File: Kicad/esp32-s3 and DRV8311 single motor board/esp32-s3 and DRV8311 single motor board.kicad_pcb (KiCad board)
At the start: 4 copper layers, 38.8 x 40.3 mm, 90 parts, among them J1 JST SH SM04B, J2 7 pin FPC 0.3mm, J3 Molex_PicoBlade_53048-0310 Ho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, Q3 PMOS,Si7157DP, Q4 PMOS, SW1 SW_Push, SW2 SW_Push, U1 AP2112K-3.3, U2 DRV8311HRRWR, U4 BQ25060, U5 ESP32-S3, U6 74HC595, Y1 40mhz, 10ppm

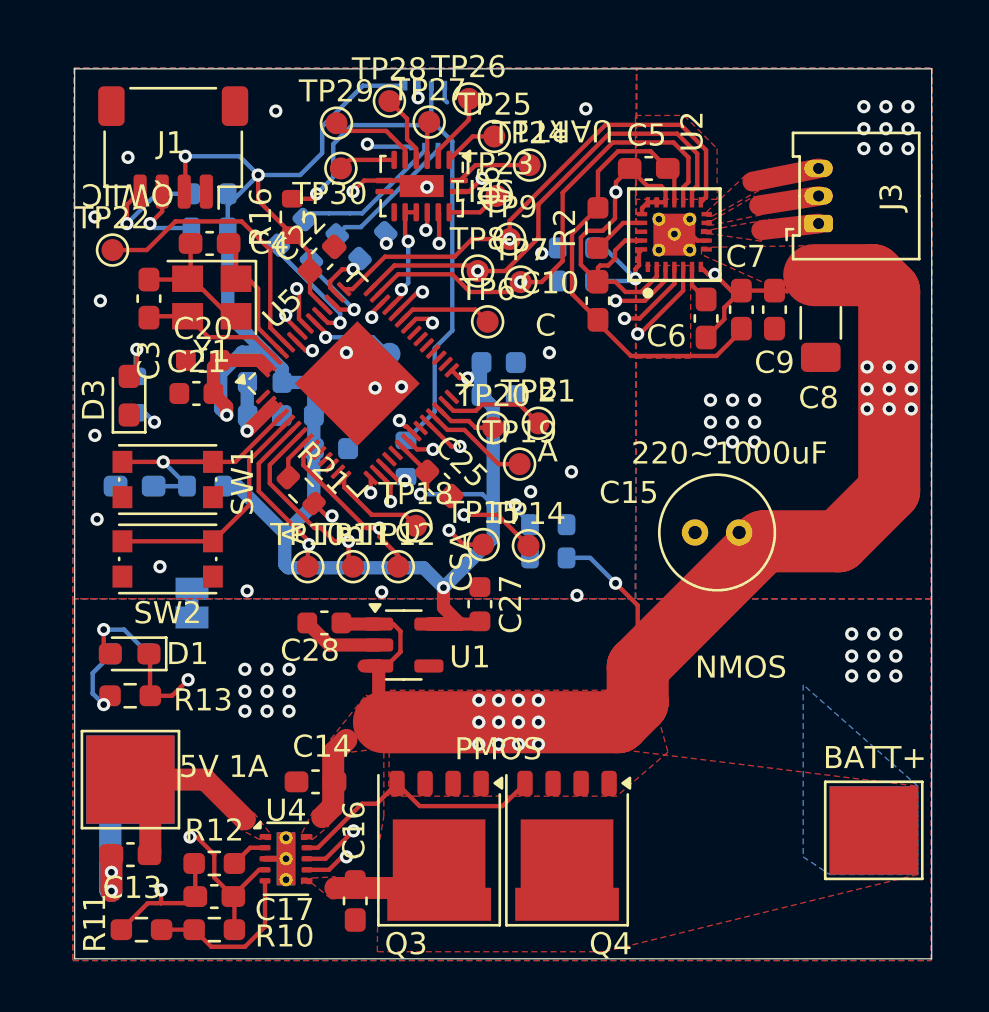
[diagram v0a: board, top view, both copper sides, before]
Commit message: Fixed Silkscreen
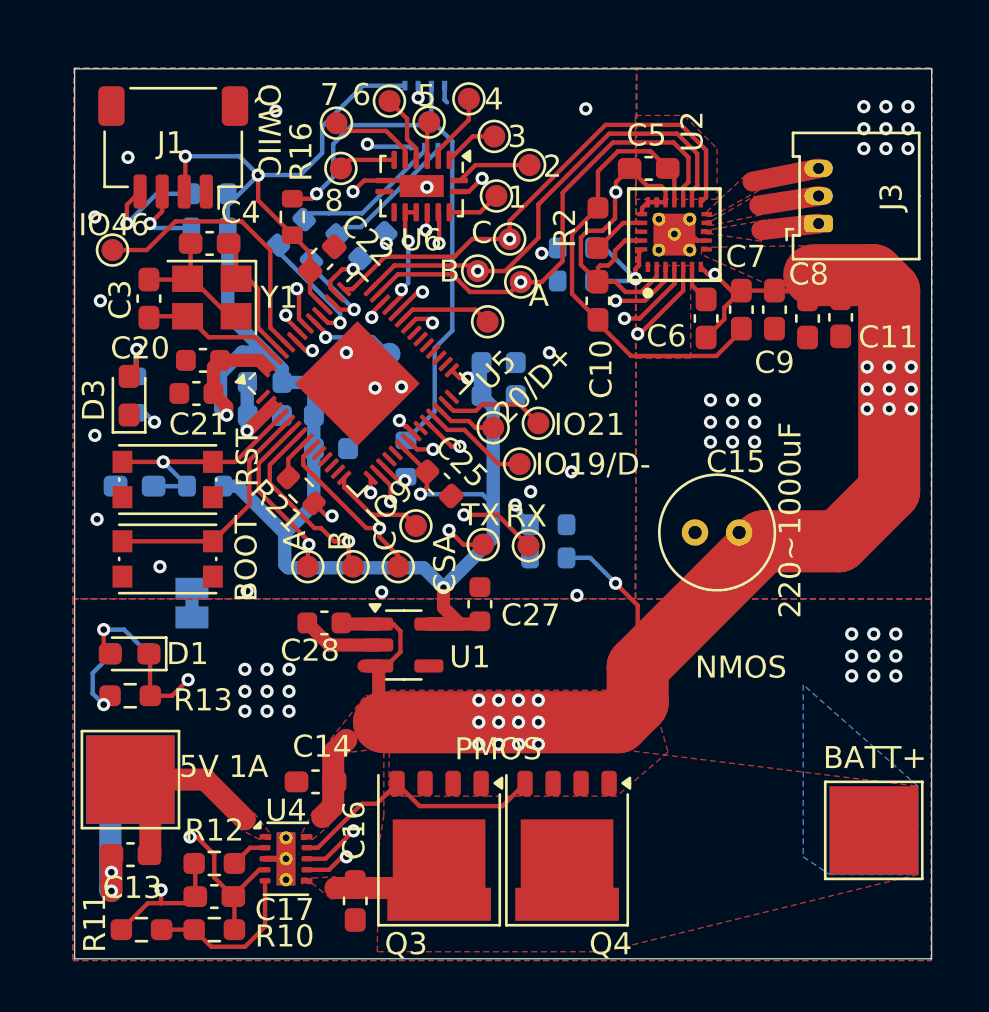
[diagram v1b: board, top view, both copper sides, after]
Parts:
- added C11: 22uF, Capacitor_SMD:C_0603_1608Metric_Pad1.08x0.95mm_HandSolder, F.Cu at (157.4, 101.2)
- C8: value 220uF, 16 v -> 22uF; footprint Capacitor_SMD:C_1206_3216Metric_Pad1.33x1.80mm_HandSolder -> Capacitor_SMD:C_0603_1608Metric_Pad1.08x0.95mm_HandSolder
- moved C8 0.63 mm to (155.9, 101.2)
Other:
- board text added: "1"
- board text added: "2"
- board text added: "20/D+"
- board text added: "3"
- board text added: "4"
- board text added: "5"
- board text added: "6"
- board text added: "7"
- board text added: "8"
- board text added: "BOOT"
- board text added: "CS0"
- board text added: "Contacts facing PCB"
- board text added: "ESP32-s3 motor pcb V2"
- board text added: "Encoder FPC"
- board text added: "IO19/D-"
- board text added: "IO21"
- board text added: "IO46"
- board text added: "IO9"
- board text removed: "ADC11"
- board text removed: "CS1"
- board text removed: "MISO"
- board text removed: "MOSI"
- board text removed: "SCK"
- board text removed: "SPI1"
- board text removed: "SWC"
- board text removed: "SWD"
- board text removed: "UART1"
- board text removed: "V1 Alpha single brushless PCB"

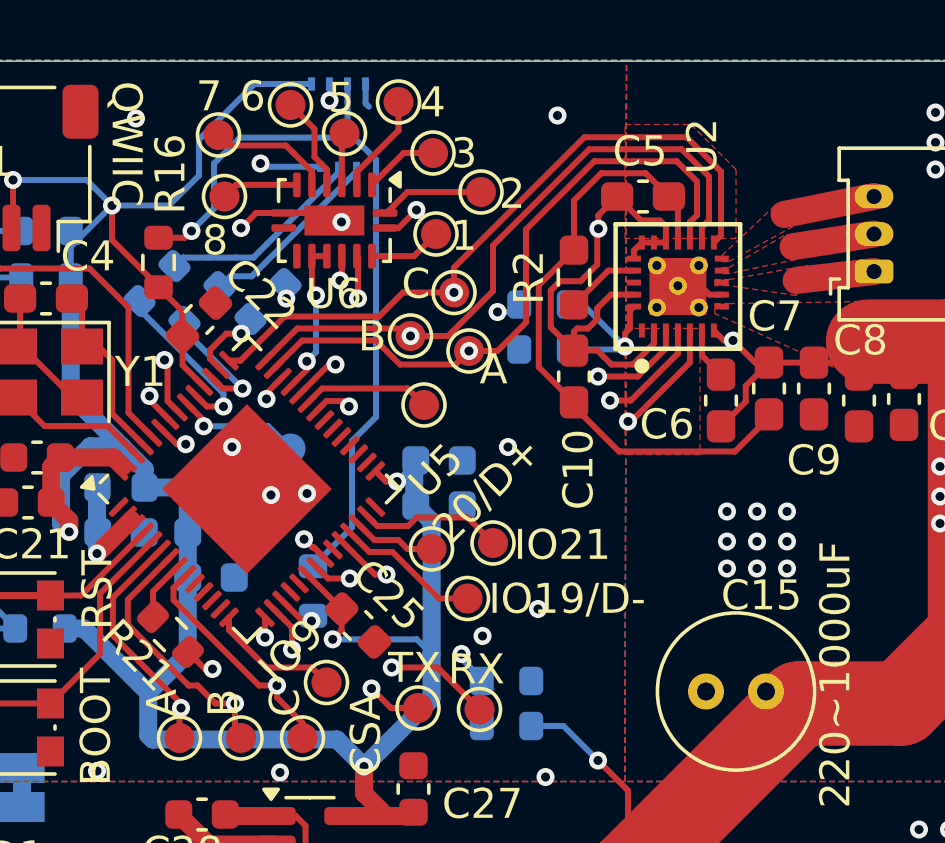
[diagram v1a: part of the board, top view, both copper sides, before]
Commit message: Switched Shift register lines to USB
The shift register will be virtually unaffected by any USB activity, and the usb lines should not be affected at low speeds for having a shift register on the bus. In my final design I will be using every last pin, so I need to use the USB lines for something. This seemed like the most logical choice, since outputs have a dedicated enable line. I can disable USB entirely as well and just program over JTAG/ encoder SPI bus.
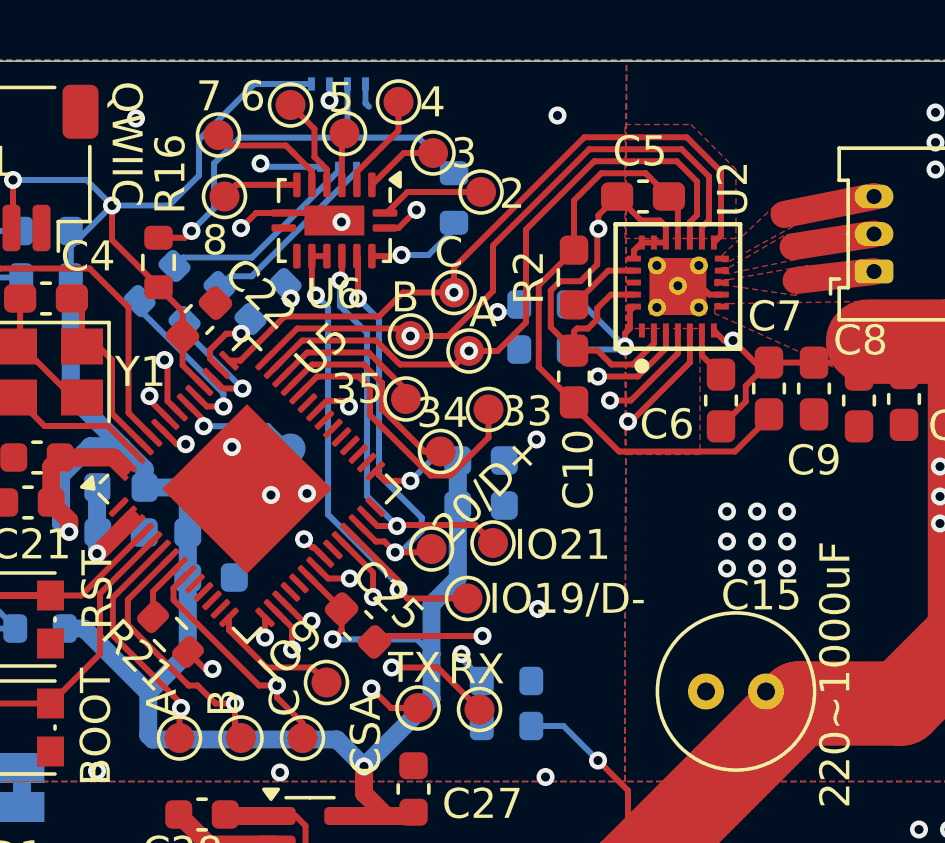
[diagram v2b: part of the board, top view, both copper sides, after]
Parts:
- removed TP23, TP6: ~, TestPoint:TestPoint_Pad_D1.0mm
- added TP2: ~, TestPoint:TestPoint_Pad_D1.0mm, F.Cu at (143.6, 101.5)
- added TP3: ~, TestPoint:TestPoint_Pad_D1.0mm, F.Cu at (141.9, 102.9)
- added TP4: ~, TestPoint:TestPoint_Pad_D1.0mm, F.Cu at (140.8, 101.2)
- moved R6 13.9 mm to (142.4, 94.5)
- moved C23 1.40 mm to (143.3, 103.2)
- moved C24 1.40 mm to (143.3, 104.7)
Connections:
- R6 pad 2: Net-(U5-GPIO12) -> Net-(U6-QA)
- U5 pad 17: Net-(U5-GPIO12) -> unconnected-(U5-GPIO12-Pad17)
- U5 pad 18: /CS2 -> unconnected-(U5-GPIO13-Pad18)
- U5 pad 19: /CS3 -> unconnected-(U5-GPIO14-Pad19)
- U5 pad 23: /CS4 -> unconnected-(U5-GPIO17-Pad23)
- U5 pad 37: Net-(U5-SPICLK_P) -> unconnected-(U5-SPICLK_P-Pad37)
- U6 pad 11: Net-(U5-GPIO34) -> Net-(U5-GPIO19/USB_D-)
- U6 pad 12: Net-(U5-GPIO34) -> Net-(U5-GPIO19/USB_D-)
- U6 pad 13: Net-(U5-GPIO35) -> Net-(U5-GPIO21)
- U6 pad 14: Net-(U5-GPIO33) -> Net-(U5-GPIO20/USB_D+)
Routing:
- net Net-(U5-GPIO19/USB_D-): track 4.83 -> 17.8 mm, vias 0 -> 2
- net /CS1: track 26.1 -> 14.5 mm
- net Net-(U5-GPIO20/USB_D+): track 2.78 -> 14.1 mm, vias 0 -> 2
- net Net-(U5-GPIO21): track 4.82 -> 14.4 mm, vias 0 -> 2
- net Net-(U5-GPIO33): track 5.57 -> 9.92 mm, vias 2 -> 0
- net Net-(U5-SPICLK_P): track 4.31 -> 0.00 mm
- net GND: track 69.0 -> 72.7 mm
- net Net-(U5-GPIO35): track 7.49 -> 5.30 mm, vias 2 -> 0
- net Net-(U5-GPIO34): track 5.24 -> 7.01 mm, vias 2 -> 0
- net VDD: track 102.3 -> 103.8 mm
- net unconnected-(U5-GPIO12-Pad17): track 0.00 -> 1.46 mm, vias 0 -> 1
- net Net-(U5-GPIO12): track 1.46 -> 0.00 mm, vias 1 -> 0
- net Net-(U6-QA): track 2.44 -> 3.33 mm, vias 0 -> 1
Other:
- board text added: "33"
- board text added: "34"
- board text added: "35"
- board text removed: "1"
